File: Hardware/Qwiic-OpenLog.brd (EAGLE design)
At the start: 38.1 x 38.1 mm, 33 parts, among them J1 MICRO-SD, J10 GATOR, J5 ISP, J7 GATOR, J8 GATOR, J9 GATOR, Q1 16MHZ, U2 ATMEGA328P

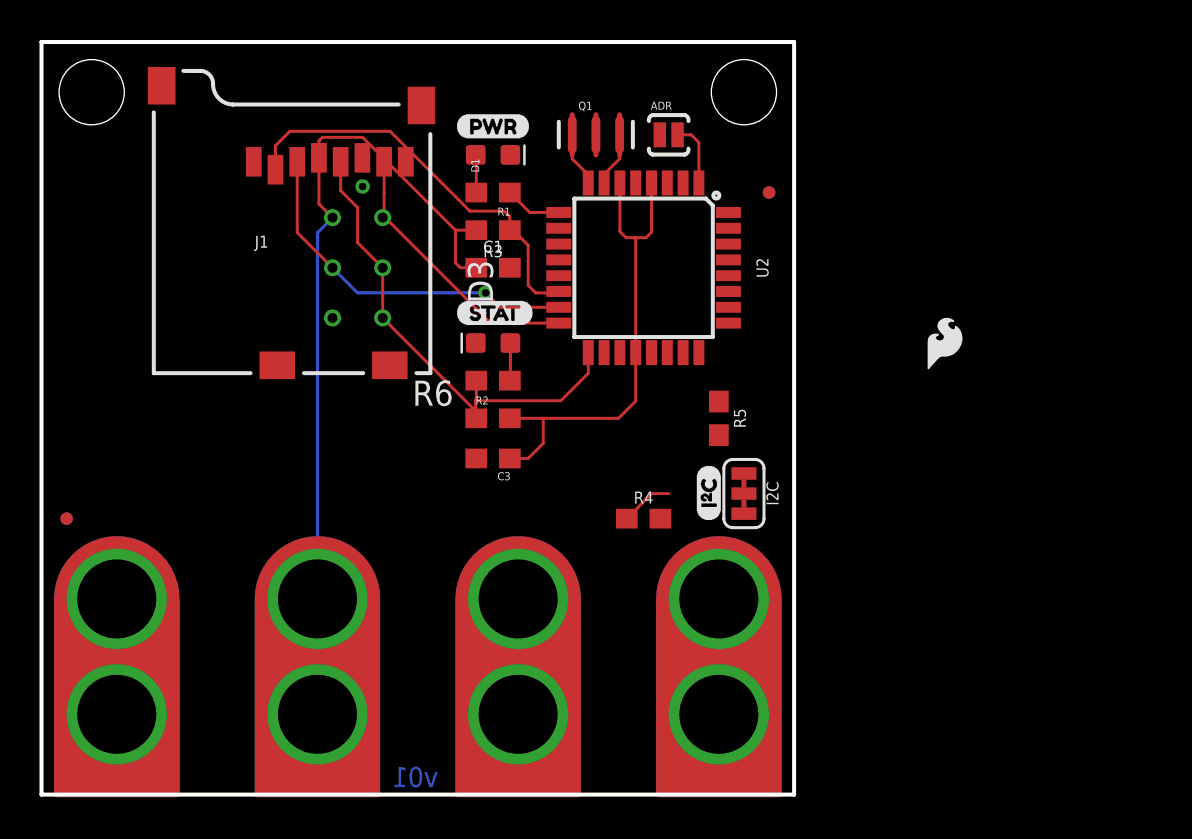
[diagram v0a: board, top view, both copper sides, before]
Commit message: initial layout completed, needs silk
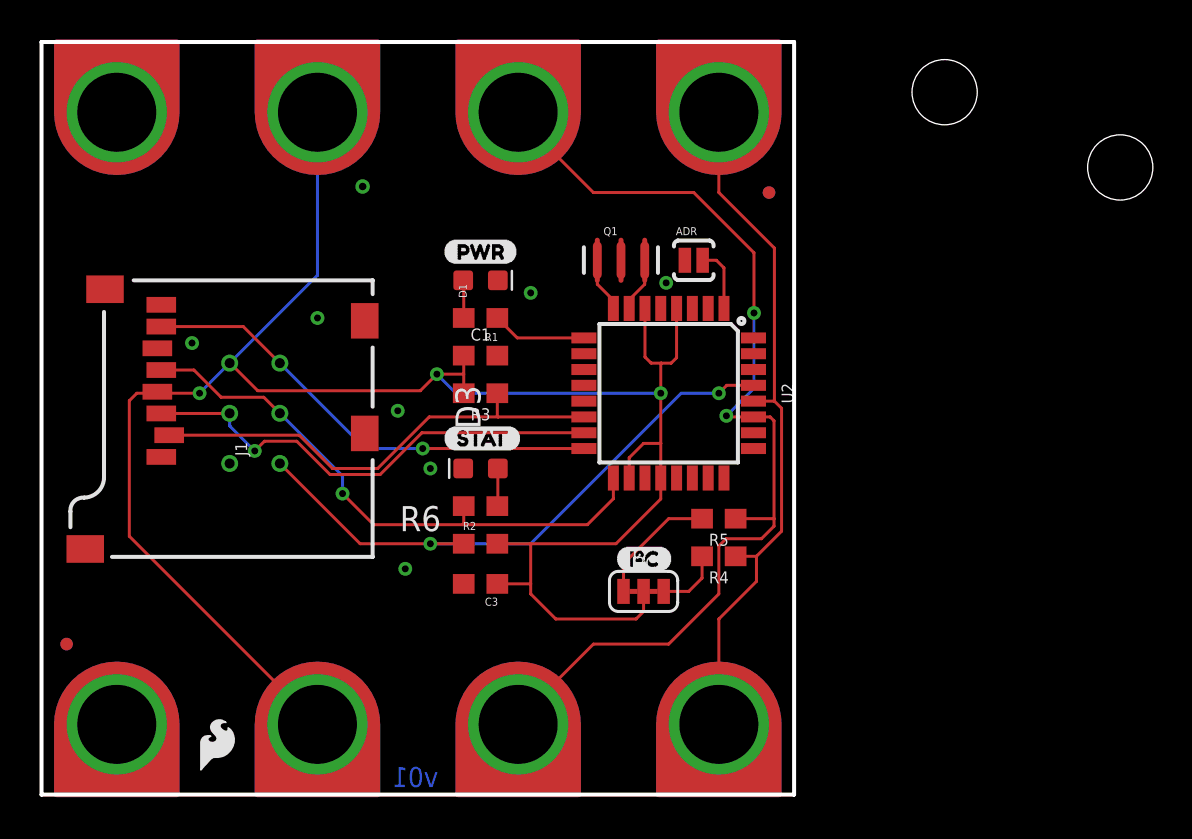
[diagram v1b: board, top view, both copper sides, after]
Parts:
- added J2, J3, J4, J6: GATORGATOR_MINI, SparkFun-Connectors:GATOR_MINI
- J10, J7, J8, J9: value GATOR -> GATORGATOR_MINI; device SparkFun-Connectors:GATOR -> SparkFun-Connectors:GATOR_MINI
- moved JP3 52.2 mm to (54.6, 31.8)
- moved LOGO1 42.1 mm to (8.89, 2.54)
- moved LOGO2 32.5 mm to (19.1, 1.27)
- moved LOGO4 10.9 mm to (45.0, 21.6)
- moved JP4 10.2 mm to (45.7, 35.6)
- moved J5 9.02 mm to (10.8, 19.3)
- moved R3 8.28 mm to (22.2, 20.3)
- moved I2C 7.09 mm to (30.5, 10.3), turned to 0 degrees
- moved ADR 6.48 mm to (33.0, 27.1)
- moved Q1 6.48 mm to (29.3, 27.1)
- moved U2 6.48 mm to (31.8, 20.3)
- moved C3 6.38 mm to (22.2, 10.7)
- moved R1 6.38 mm to (22.2, 24.1)
- moved R2 6.38 mm to (22.2, 12.7)
- moved U$17 6.38 mm to (20.3, 18.0)
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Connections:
- net 3.3V: now also J4.P$2; no longer J9.P$1
- net GND: now also J6.P$2; no longer J10.P$1
- net SCL: now also J2.P$2; no longer J7.P$1
- net SDA: now also J3.P$2; no longer J8.P$1
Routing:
- net SDA: track 0.00 -> 52.3 mm, vias 0 -> 2
- net 3.3V: track 61.7 -> 104.7 mm, vias 0 -> 3
- net SCL: track 2.65 -> 35.7 mm
- net RST: track 0.00 -> 30.7 mm, vias 0 -> 2
- net MISO: track 13.9 -> 24.0 mm, vias 0 -> 1
- net N$5: track 0.00 -> 6.32 mm
- net MOSI: track 18.4 -> 24.3 mm
- net SCK: track 24.3 -> 29.2 mm, vias 0 -> 1
- net N$6: track 0.00 -> 3.33 mm
- net CS: track 20.9 -> 24.1 mm
- net N$4: track 2.90 -> 4.80 mm

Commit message: adding RTC
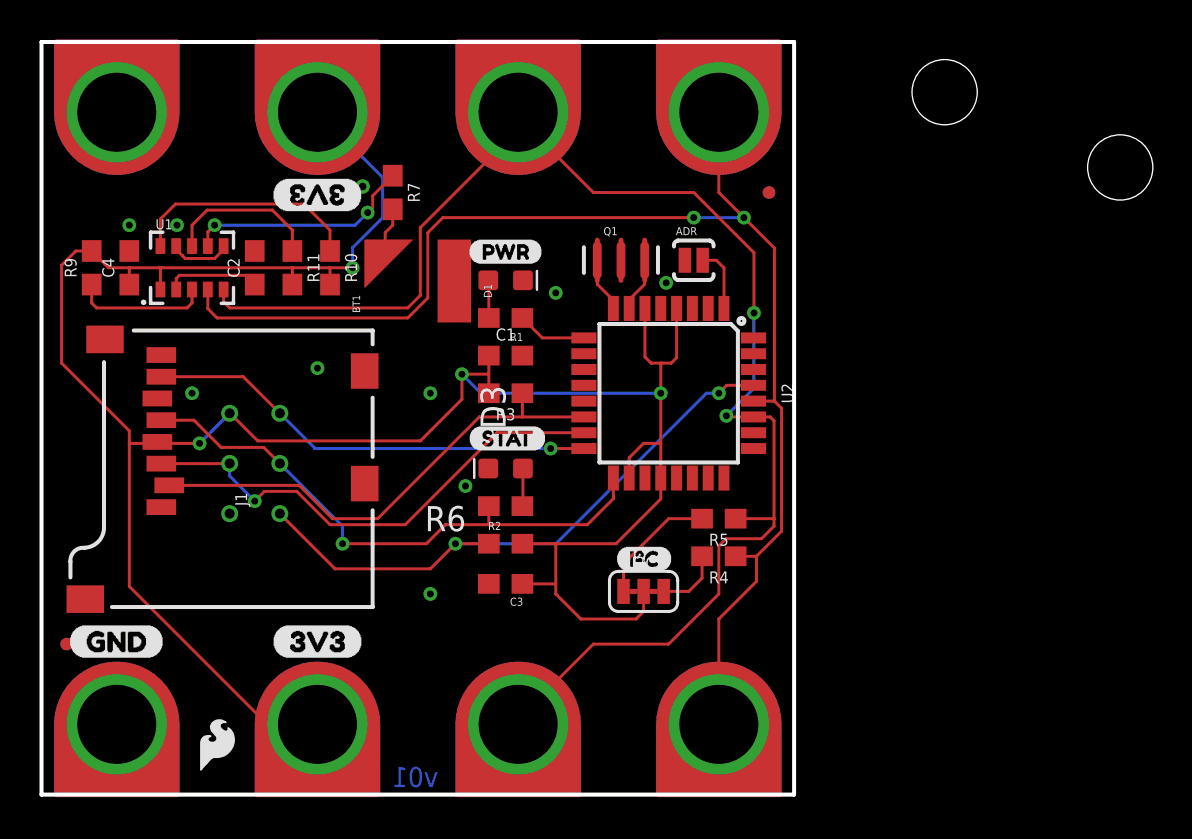
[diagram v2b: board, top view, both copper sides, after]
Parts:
- added BT1: ML414H_IV01E_BATTERY, SparkFun-Batteries:ML414H_IV01E
- added C2: 47pF, SparkFun-Capacitors:0603
- added C4: 10nF, SparkFun-Capacitors:0603
- added R10, R11, R9: 10k, SparkFun-Resistors:0603
- added R7: 1k, SparkFun-Resistors:0603
- added U$1, U$3: (no value), buzzard_labels:3V33
- added U$2: (no value), buzzard_labels:GND0
- added U1: RV-1805, SparkFun-Clocks:RV-1805
- moved J1 2.54 mm to (16.8, 23.5)
- moved J5 2.54 mm to (10.8, 16.8)
- moved C1 1.27 mm to (23.5, 22.2)
- moved C3 1.27 mm to (23.5, 10.7)
- moved D1 1.27 mm to (23.5, 26.0)
- moved D3 1.27 mm to (23.5, 16.5)
- moved R1 1.27 mm to (23.5, 24.1)
- moved R2 1.27 mm to (23.5, 12.7)
- moved R3 1.27 mm to (23.5, 20.3)
- moved R6 1.27 mm to (23.5, 14.6)
- moved U$17 1.27 mm to (21.6, 18.0)
- moved U$9 1.27 mm to (21.6, 27.5)
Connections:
- new net !INT: R9.1, U1.3
- new net !RST: R10.1, U1.10
- new net N$10: C2.1, U1.2
- new net N$8: BT1.+, R7.2
- new net PSW: R11.1, U1.8
- new net VBACKUP: R7.1, U1.7
- net 3.3V: now also C4.1, R10.2, R11.2, R9.2, U1.1
- net GND: now also BT1.-, C2.2, C4.2, U1.6, U1.9
- net SCL: now also U1.4
- net SDA: now also U1.5
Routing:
- net SCL: track 35.7 -> 68.1 mm, vias 0 -> 2
- net 3.3V: track 104.7 -> 128.0 mm, vias 3 -> 4
- net SDA: track 52.3 -> 74.4 mm
- net !RST: track 0.00 -> 11.9 mm
- net VBACKUP: track 0.00 -> 11.6 mm, vias 0 -> 2
- net PSW: track 0.00 -> 7.93 mm
- net !INT: track 0.00 -> 6.90 mm
- net N$10: track 0.00 -> 4.79 mm
- net GND: track 0.00 -> 3.12 mm, vias 8 -> 10
- net N$8: track 0.00 -> 3.01 mm
- net N$4: track 4.80 -> 3.53 mm
- net MOSI: track 24.3 -> 25.4 mm
- net MISO: track 24.0 -> 22.9 mm
- net CS: track 24.1 -> 25.0 mm

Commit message: updating silk, adding rtc
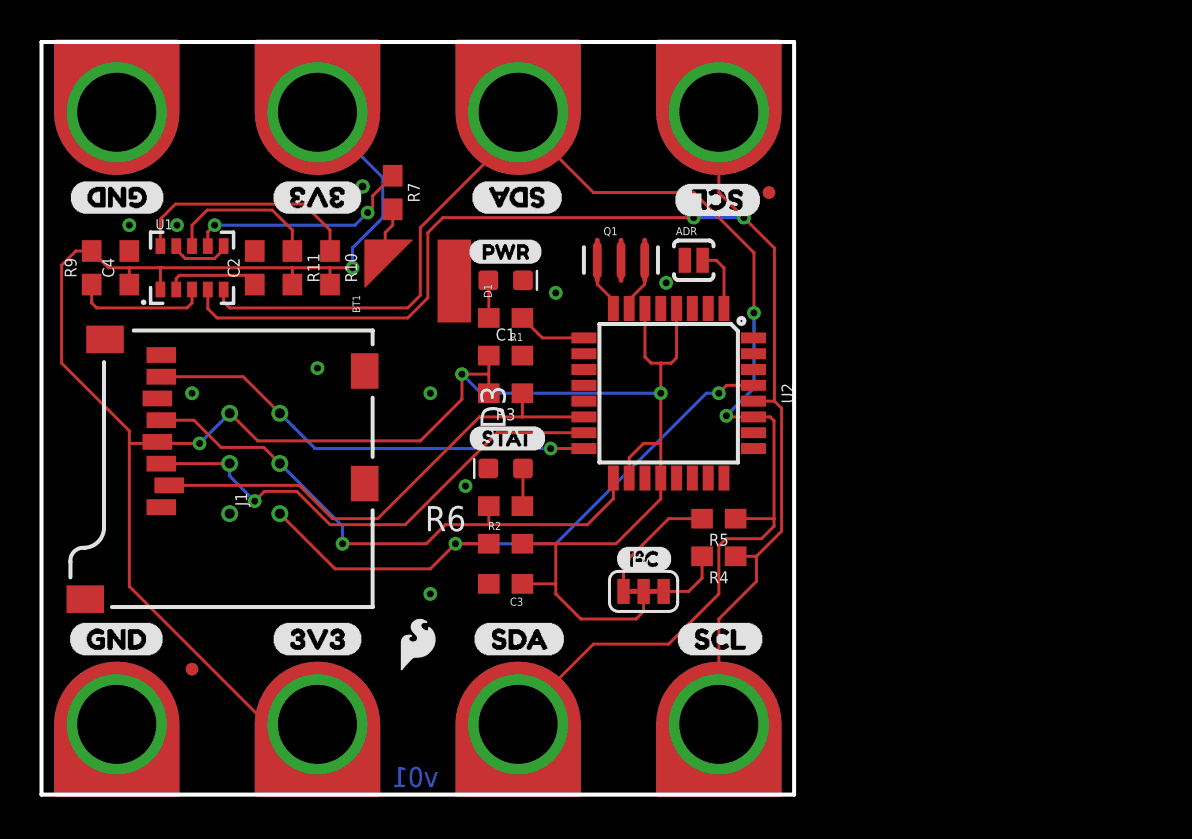
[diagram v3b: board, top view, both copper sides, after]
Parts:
- removed JP3, JP4: STAND-OFF, SparkFun:STAND-OFF
- added U$10, U$11: (no value), buzzard_labels:GND0
- added U$12, U$15: (no value), buzzard_labels:3V33
- added U$13, U$16, U$4, U$7: (no value), buzzard_labels:SDA1
- added U$14, U$18, U$5, U$6: (no value), buzzard_labels:SCL2
- moved LOGO4 26.3 mm to (19.1, 17.0), turned to 0 degrees
- moved LOGO1 11.4 mm to (19.1, 7.62)
- moved FID2 6.48 mm to (7.62, 6.35)
- moved FID3 6.48 mm to (7.62, 6.35)
- moved U$3 0.13 mm to (16.3, 30.2)
- moved U$1 0.13 mm to (11.6, 7.87)
- moved U$2 0.13 mm to (1.37, 7.87)
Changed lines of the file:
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@@
 </element>
 <element name="FID1" library="SparkFun-Aesthetics" package="FIDUCIAL-MICRO" value="FIDUCIALUFIDUCIAL" x="36.83" y="30.48" smashed="yes"/>
-<element name="FID2" library="SparkFun-Aesthetics" package="FIDUCIAL-MICRO" value="FIDUCIALUFIDUCIAL" x="1.27" y="7.62" smashed="yes"/>
+<element name="FID2" library="SparkFun-Aesthetics" package="FIDUCIAL-MICRO" value="FIDUCIALUFIDUCIAL" x="7.62" y="6.35" smashed="yes"/>
 <element name="LOGO2" library="SparkFun-Aesthetics" package="OSHW-LOGO-MINI" value="OSHW-LOGOMINI" x="19.05" y="1.27" smashed="yes" rot="MR0"/>
-<element name="FID3" library="SparkFun-Aesthetics" package="FIDUCIAL-MICRO" value="FIDUCIALUFIDUCIAL" x="1.27" y="7.62" smashed="yes" rot="MR180"/>
+<element name="FID3" library="SparkFun-Aesthetics" package="FIDUCIAL-MICRO" value="FIDUCIALUFIDUCIAL" x="7.62" y="6.35" smashed="yes" rot="MR180"/>
 <element name="FID4" library="SparkFun-Aesthetics" package="FIDUCIAL-MICRO" value="FIDUCIALUFIDUCIAL" x="36.83" y="30.48" smashed="yes" rot="MR0"/>
 <element name="C1" library="SparkFun-Capacitors" package="0603" value="4.7uF" x="23.495" y="22.225" smashed="yes">
@@
 <attribute name="VALUE" x="30.48" y="9.144" size="0.6096" layer="27" font="vector" ratio="20" align="top-center"/>
 </element>
-<element name="JP3" library="SparkFun" package="STAND-OFF" value="STAND-OFF" x="54.61" y="31.75" smashed="yes"/>
-<element name="JP4" library="SparkFun" package="STAND-OFF" value="STAND-OFF" x="45.72" y="35.56" smashed="yes" rot="R90"/>
 <element name="J5" library="SparkFun-Connectors" package="2X3_TEST_POINTS" value="ISP" x="10.795" y="16.764" smashed="yes" rot="MR270">
 <attribute name="NAME" x="8.763" y="19.812" size="0.6096" layer="26" font="vector" ratio="20" rot="MR270"/>
@@
 <attribute name="VALUE" x="11.684" y="14.605" size="0.6096" layer="27" font="vector" ratio="20" rot="R90"/>
 </element>
-<element name="LOGO4" library="SparkFun-Aesthetics" package="SFE_LOGO_NAME_FLAME_.1" value="SFE_LOGO_NAME_FLAME.1_INCH" x="44.958" y="21.59" smashed="yes" rot="MR90"/>
-<element name="LOGO1" library="SparkFun-Aesthetics" package="SFE_LOGO_FLAME_.1" value="SFE_LOGO_FLAME.1_INCH" x="8.89" y="2.54" smashed="yes"/>
+<element name="LOGO4" library="SparkFun-Aesthetics" package="SFE_LOGO_NAME_FLAME_.1" value="SFE_LOGO_NAME_FLAME.1_INCH" x="19.05" y="17.018" smashed="yes" rot="MR0"/>
+<element name="LOGO1" library="SparkFun-Aesthetics" package="SFE_LOGO_FLAME_.1" value="SFE_LOGO_FLAME.1_INCH" x="19.05" y="7.62" smashed="yes"/>
 <element name="J7" library="SparkFun-Connectors" package="GATOR_MINI" value="GATORGATOR_MINI" x="34.29" y="3.81" smashed="yes"/>
 <element name="J8" library="SparkFun-Connectors" package="GATOR_MINI" value="GATORGATOR_MINI" x="24.13" y="3.81" smashed="yes"/>
@@
 <attribute name="VALUE" x="11.938" y="26.67" size="0.6096" layer="27" font="vector" ratio="20" rot="R270" align="top-center"/>
 </element>
-<element name="U$1" library="buzzard_labels" package="3V33" value="" x="11.6332" y="7.747" smashed="yes"/>
-<element name="U$2" library="buzzard_labels" package="GND0" value="" x="1.3716" y="7.747" smashed="yes"/>
+<element name="U$1" library="buzzard_labels" package="3V33" value="" x="11.6332" y="7.874" smashed="yes"/>
+<element name="U$2" library="buzzard_labels" package="GND0" value="" x="1.3716" y="7.874" smashed="yes"/>
 <element name="BT1" library="SparkFun-Batteries" package="ML414H_IV01E" value="ML414H_IV01E_BATTERY" x="19.05" y="25.4" smashed="yes" rot="R90">
 <attribute name="NAME" x="16.129" y="24.384" size="0.381" layer="25" rot="R90"/>
@@
 <attribute name="VALUE" x="17.018" y="30.48" size="0.6096" layer="27" font="vector" ratio="20" rot="R270" align="top-center"/>
 </element>
-<element name="U$3" library="buzzard_labels" package="3V33" value="" x="16.3068" y="30.353" smashed="yes" rot="R180"/>
+<element name="U$3" library="buzzard_labels" package="3V33" value="" x="16.3068" y="30.226" smashed="yes" rot="R180"/>
+<element name="U$4" library="buzzard_labels" package="SDA1" value="" x="21.844" y="7.874" smashed="yes"/>
+<element name="U$5" library="buzzard_labels" package="SCL2" value="" x="32.131" y="7.874" smashed="yes"/>
+<element name="U$6" library="buzzard_labels" package="SCL2" value="" x="36.449" y="30.099" smashed="yes" rot="R180"/>
+<element name="U$7" library="buzzard_labels" package="SDA1" value="" x="26.416" y="30.226" smashed="yes" rot="R180"/>
+<element name="U$10" library="buzzard_labels" package="GND0" value="" x="6.2484" y="30.226" smashed="yes" rot="R180"/>
+<element name="U$11" library="buzzard_labels" package="GND0" value="" x="1.3716" y="30.226" smashed="yes" rot="MR180"/>
+<element name="U$12" library="buzzard_labels" package="3V33" value="" x="11.6332" y="30.226" smashed="yes" rot="MR180"/>
+<element name="U$13" library="buzzard_labels" package="SDA1" value="" x="21.844" y="30.226" smashed="yes" rot="MR180"/>
+<element name="U$14" library="buzzard_labels" package="SCL2" value="" x="32.131" y="30.226" smashed="yes" rot="MR180"/>
+<element name="U$15" library="buzzard_labels" package="3V33" value="" x="16.3068" y="7.874" smashed="yes" rot="MR0"/>
+<element name="U$16" library="buzzard_labels" package="SDA1" value="" x="26.416" y="7.874" smashed="yes" rot="MR0"/>
+<element name="U$18" library="buzzard_labels" package="SCL2" value="" x="36.449" y="7.874" smashed="yes" rot="MR0"/>
 </elements>
 <signals>
